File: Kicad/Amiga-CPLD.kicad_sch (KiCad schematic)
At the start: 23 parts, among them CN1 CDTV-DIAG, J1 Conn_01x06_Male, U1 AZ1117-3.3, U2 XC95144XL-TQ100, X1 50MHz

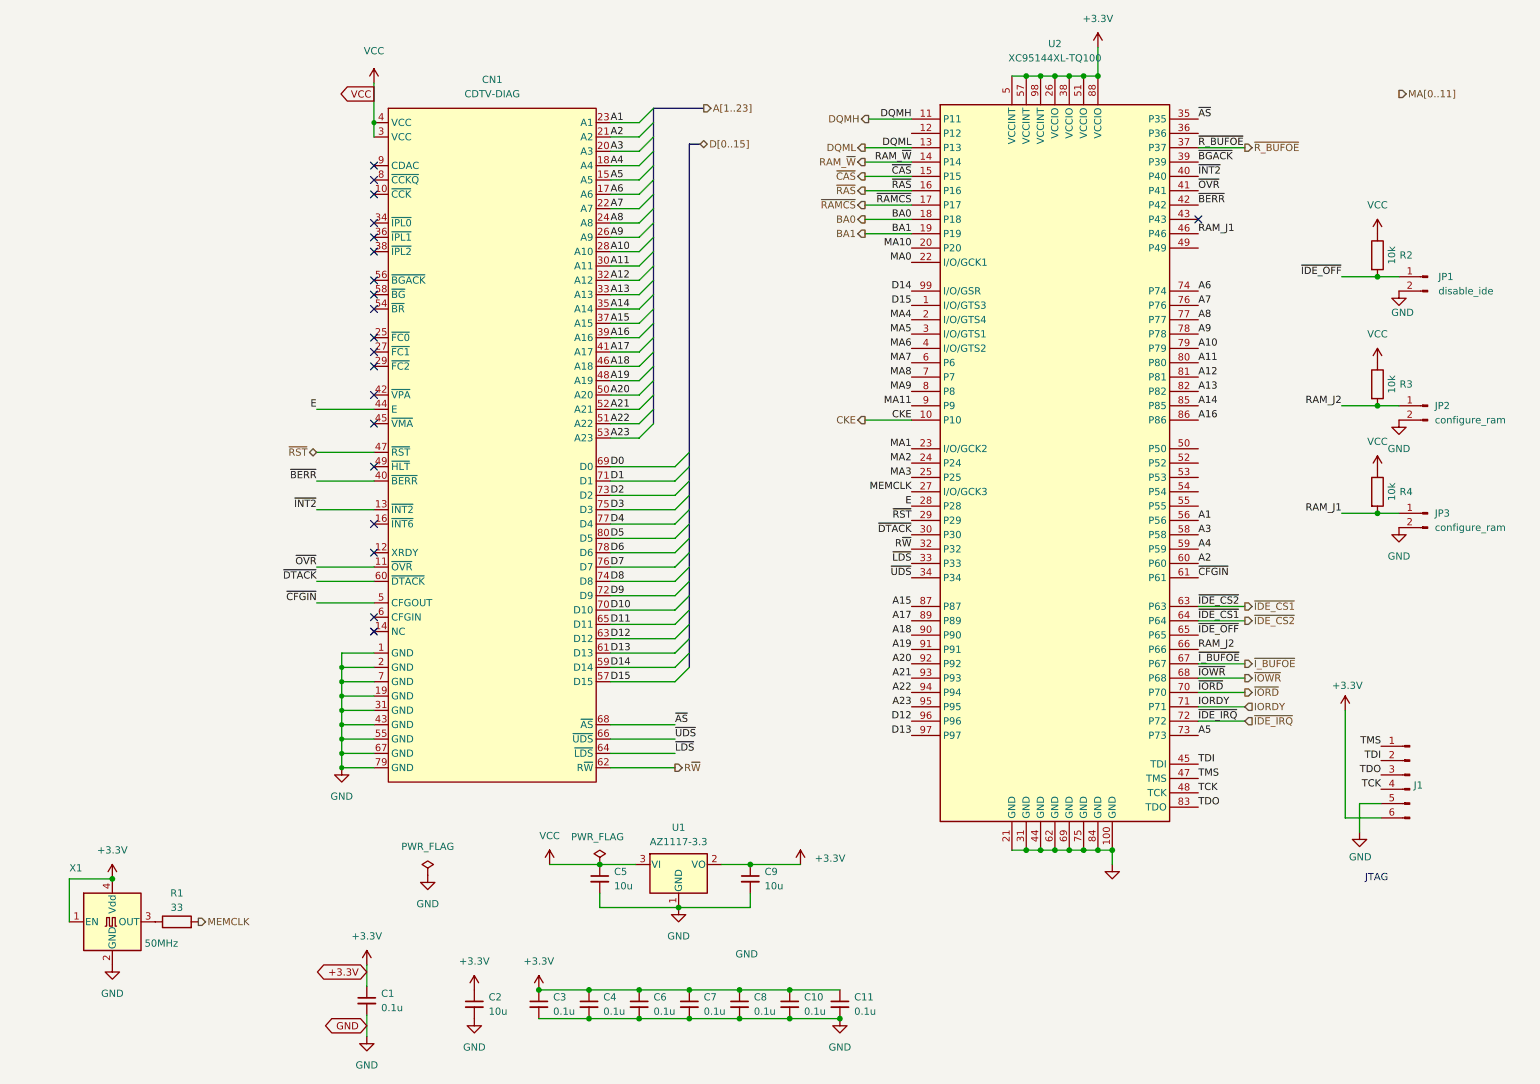
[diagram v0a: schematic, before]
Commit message: PCB: Add 39SF010 for IDE ROM
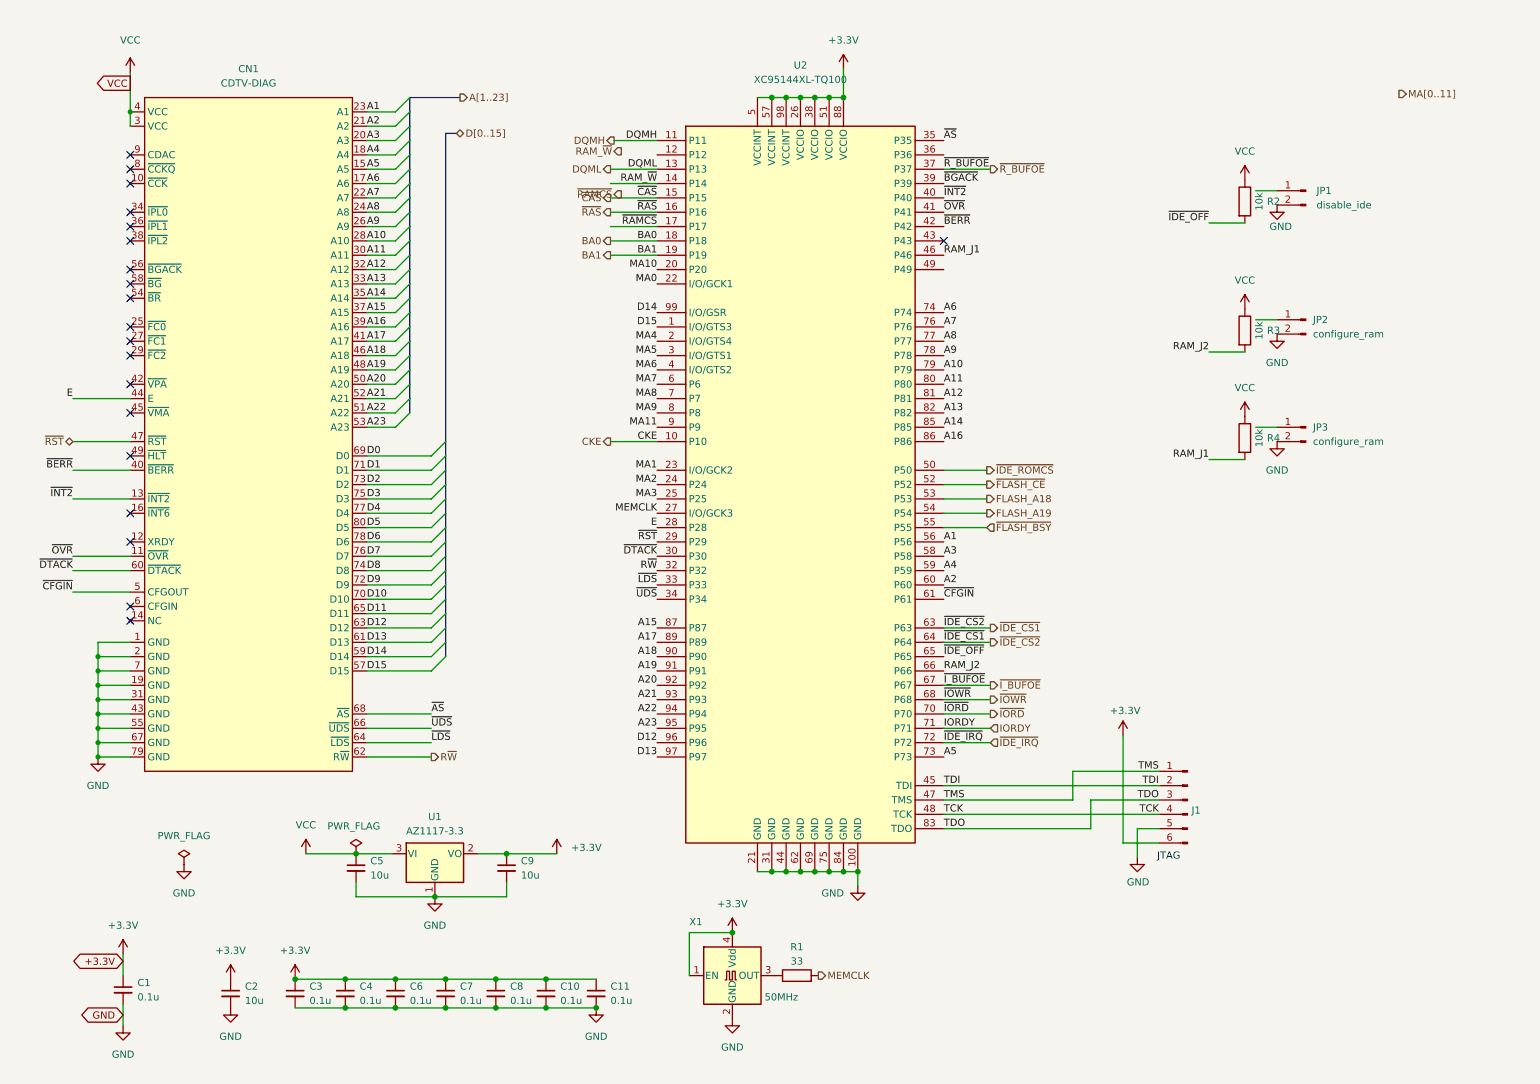
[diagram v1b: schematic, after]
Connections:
- net RAM_J1: no longer JP3.1 (Pin_1)
- net RAM_J2: no longer JP2.1 (Pin_1)
- net ~{IDE_OFF}: no longer JP1.1 (Pin_1)
- net ~{IDE_ROMCS}: now reaches U2.50 (P50)
- net ~{FLASH_CE}: now reaches U2.52 (P52)
- net FLASH_A18: now reaches U2.53 (P53)
- net FLASH_A19: now reaches U2.54 (P54)
- net ~{FLASH_BSY}: now reaches U2.55 (P55)
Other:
- moved on the sheet: C1, C10, C11, C2, C3, C4, C5, C6, C7, C8, C9, CN1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

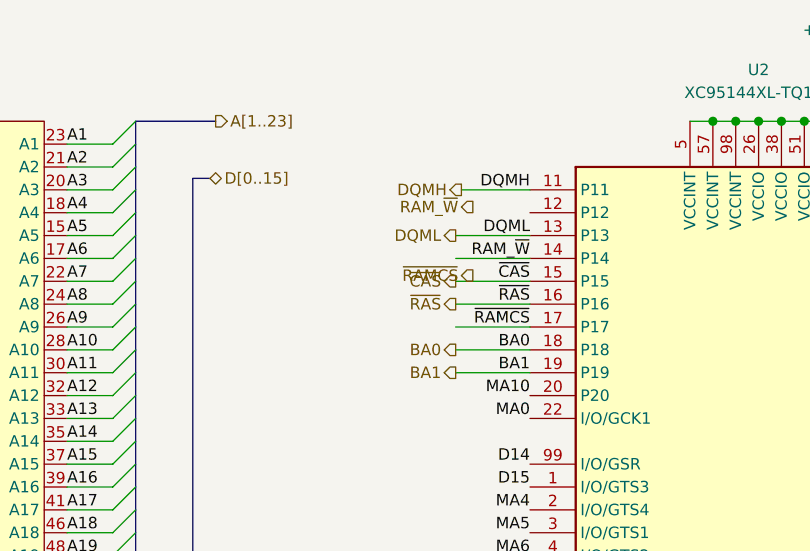
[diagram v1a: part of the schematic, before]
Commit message: PCB: Change IDE address line connections from A2-4 to A10-12 (Gayle vs AT-Apollo style IDE)
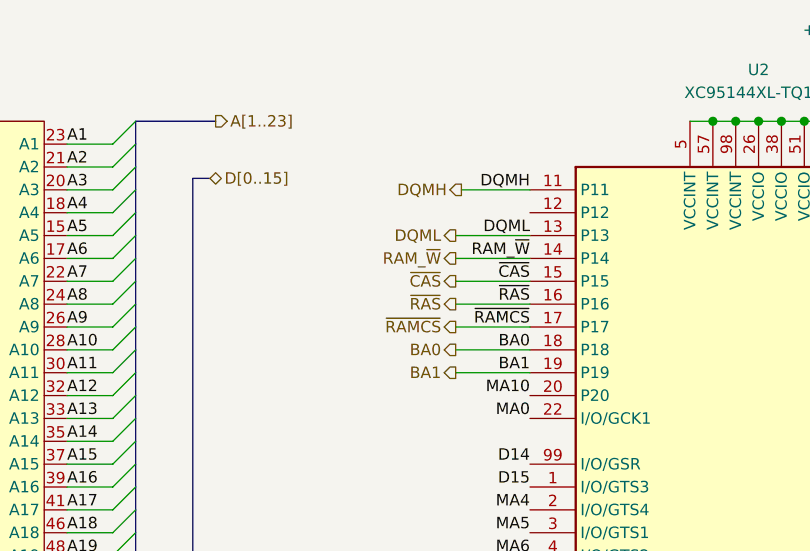
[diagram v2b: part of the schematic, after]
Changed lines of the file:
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@@
     (effects (font (size 1.27 1.27)) (justify left))
   )
-  (hierarchical_label "~{RAMCS}" (shape output) (at 126.365 41.275 180)
+  (hierarchical_label "~{RAMCS}" (shape output) (at 124.46 46.99 180)
     (effects (font (size 1.27 1.27)) (justify right))
   )
@@
     (effects (font (size 1.27 1.27)) (justify left))
   )
-  (hierarchical_label "RAM_~{W}" (shape output) (at 126.365 33.655 180)
+  (hierarchical_label "RAM_~{W}" (shape output) (at 124.46 39.37 180)
     (effects (font (size 1.27 1.27)) (justify right))
   )

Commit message: PCB: Start routing PCB
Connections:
- net A1: now also U2.90 (P90); no longer U2.56 (P56)
- net A10: now also U2.82 (P82); no longer U2.79 (P79)
- net A11: now also U2.77 (P77); no longer U2.80 (P80)
- net A12: now also U2.78 (P78); no longer U2.81 (P81)
- net A13: now also U2.80 (P80); no longer U2.82 (P82)
- net A14: now also U2.79 (P79); no longer U2.85 (P85)
- net A15: now also U2.74 (P74); no longer U2.87 (P87)
- net A16: now also U2.76 (P76); no longer U2.86 (P86)
- net A17: now also U2.73 (P73); no longer U2.89 (P89)
- net A18: now also U2.66 (P66); no longer U2.90 (P90)
- net A19: now also U2.67 (P67); no longer U2.91 (P91)
- net A2: now also U2.91 (P91); no longer U2.60 (P60)
- net A20: now also U2.63 (P63); no longer U2.92 (P92)
- net A21: now also U2.64 (P64); no longer U2.93 (P93)
- net A22: now also U2.68 (P68); no longer U2.94 (P94)
- net A23: now also U2.65 (P65); no longer U2.95 (P95)
- net A3: now also U2.89 (P89); no longer U2.58 (P58)
- net A4: now also U2.87 (P87); no longer U2.59 (P59)
- net A5: now also U2.93 (P93); no longer U2.73 (P73)
- net A6: now also U2.92 (P92); no longer U2.74 (P74)
- net A7: now also U2.85 (P85); no longer U2.76 (P76)
- net A8: now also U2.86 (P86); no longer U2.77 (P77)
- net A9: now also U2.81 (P81); no longer U2.78 (P78)
- net BA0: now also U2.32 (P32); no longer U2.18 (P18)
- net BA1: now also U2.34 (P34); no longer U2.19 (P19)
- net CKE: now also U2.28 (P28); no longer U2.10 (P10)
- net D12: now also U2.59 (P59); no longer U2.96 (P96)
- net D13: now also U2.58 (P58); no longer U2.97 (P97)
- net D14: now also U2.61 (P61); no longer U2.99 (I/O/GSR)
- net D15: now also U2.60 (P60); no longer U2.1 (I/O/GTS3)
- net DQMH: no longer U2.11 (P11)
- net DQML: no longer U2.13 (P13)
- net E: now also U2.71 (P71); no longer U2.28 (P28)
- net FLASH_A18: no longer U2.53 (P53)
- net FLASH_A19: no longer U2.54 (P54)
- net IORDY: no longer U2.71 (P71)
- net MA0: now also U2.39 (P39); no longer U2.22 (I/O/GCK1)
- net MA1: now also U2.41 (P41); no longer U2.23 (I/O/GCK2)
- net MA10: now also U2.36 (P36); no longer U2.20 (P20)
- net MA11: now also U2.33 (P33); no longer U2.9 (P9)
- net MA2: now also U2.43 (P43); no longer U2.24 (P24)
- net MA3: now also U2.49 (P49); no longer U2.25 (P25)
- net MA4: now also U2.46 (P46); no longer U2.2 (I/O/GTS4)
- net MA5: now also U2.42 (P42); no longer U2.3 (I/O/GTS1)
- net MA6: now also U2.40 (P40); no longer U2.4 (I/O/GTS2)
- net MA7: now also U2.37 (P37); no longer U2.6 (P6)
- net MA8: now also U2.50 (P50); no longer U2.7 (P7)
- net MA9: now also U2.35 (P35); no longer U2.8 (P8)
- net RAM_J1: no longer U2.46 (P46)
- net RAM_J2: no longer U2.66 (P66)
- net RAM_~{W}: no longer U2.14 (P14)
- net R~{W}: now also U2.54 (P54); no longer U2.32 (P32)
- net ~{AS}: now also U2.53 (P53); no longer U2.35 (P35)
- net ~{BERR}: now also U2.70 (P70); no longer U2.42 (P42)
- net ~{BGACK}: no longer U2.39 (P39)
- net ~{CAS}: no longer U2.15 (P15)
- net ~{CFGIN}: now also U2.95 (P95); no longer U2.61 (P61)
- net ~{DTACK}: now also U2.56 (P56); no longer U2.30 (P30)
- net ~{FLASH_BSY}: no longer U2.55 (P55)
- net ~{FLASH_CE}: no longer U2.52 (P52)
- net ~{IDE_CS1}: no longer U2.63 (P63), U2.64 (P64)
- net ~{IDE_IRQ}: no longer U2.72 (P72)
- net ~{IDE_OFF}: no longer U2.65 (P65)
- net ~{IDE_ROMCS}: no longer U2.50 (P50)
- net ~{INT2}: no longer CN1.13 (~{INT2}), U2.40 (P40)
- net ~{IORD}: no longer U2.70 (P70)
- net ~{IOWR}: no longer U2.68 (P68)
- net ~{I_BUFOE}: no longer U2.67 (P67)
- net ~{LDS}: now also U2.55 (P55); no longer U2.33 (P33)
- net ~{OVR}: now also U2.94 (P94); no longer U2.41 (P41)
- net ~{RAMCS}: now also U2.30 (P30); no longer U2.17 (P17)
- net ~{RAS}: now also U2.29 (P29); no longer U2.16 (P16)
- net ~{RST}: now also U2.72 (P72); no longer U2.29 (P29)
- net ~{R_BUFOE}: no longer U2.37 (P37)
- net ~{UDS}: now also U2.52 (P52); no longer U2.34 (P34)
- no-connect marks 20 -> 21
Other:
- moved on the sheet: C1, C10, C11, C2, C3, C4, C5, C6, C7, C8, C9, CN1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
